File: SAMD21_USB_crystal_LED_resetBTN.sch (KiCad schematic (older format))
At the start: 13 parts

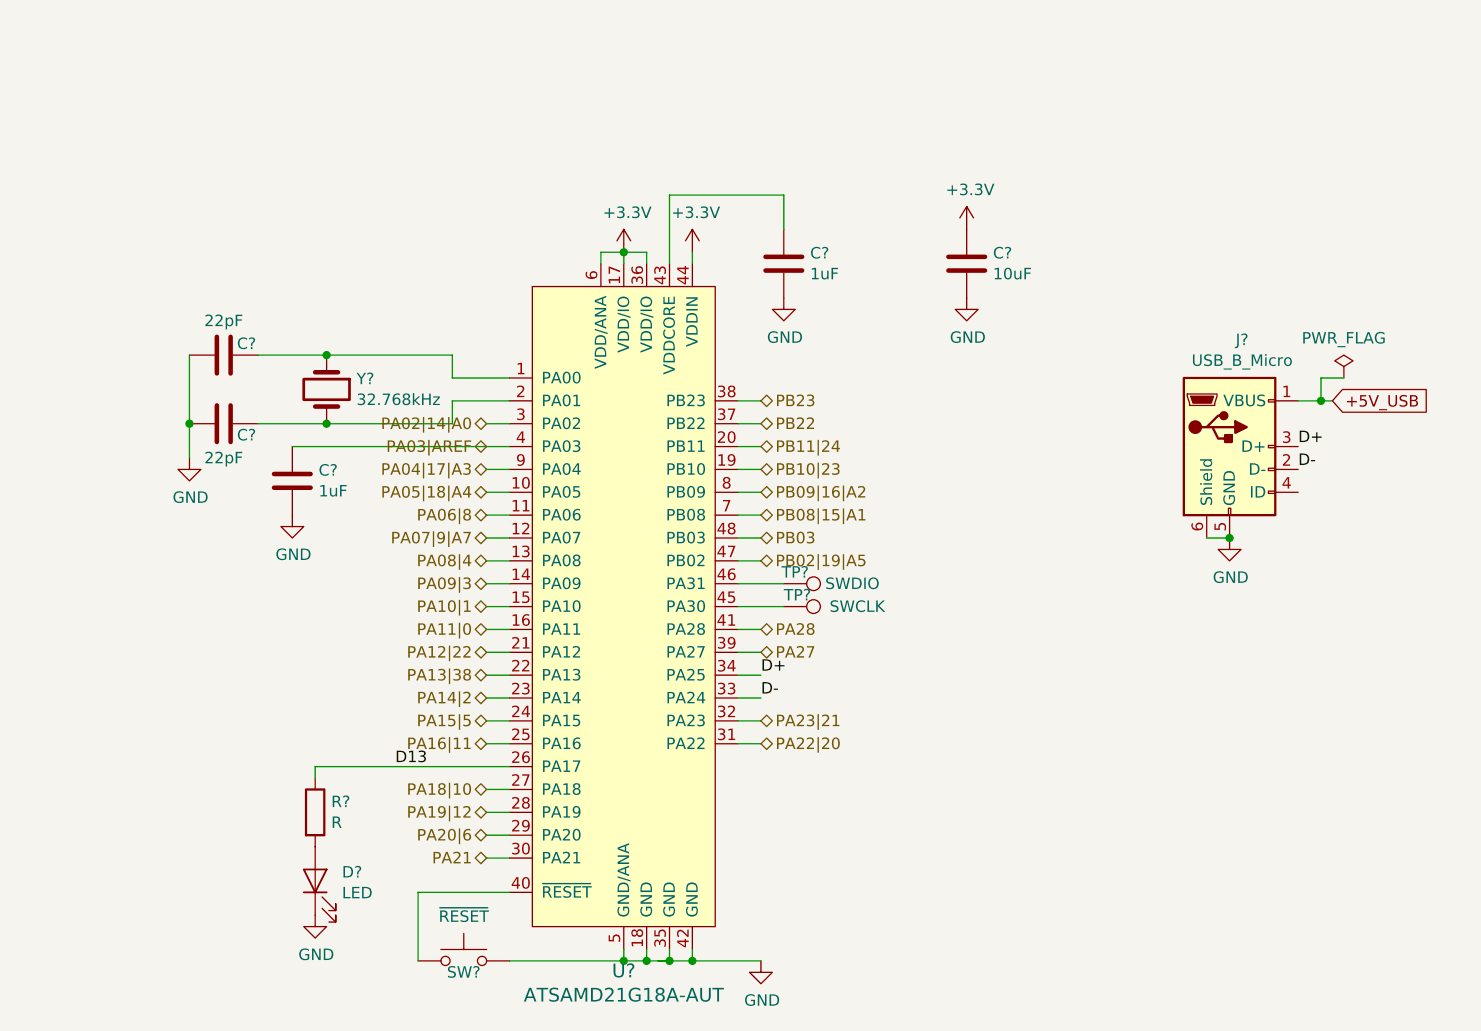
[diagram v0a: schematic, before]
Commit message: Add 3v3 LDO, annotate schematic
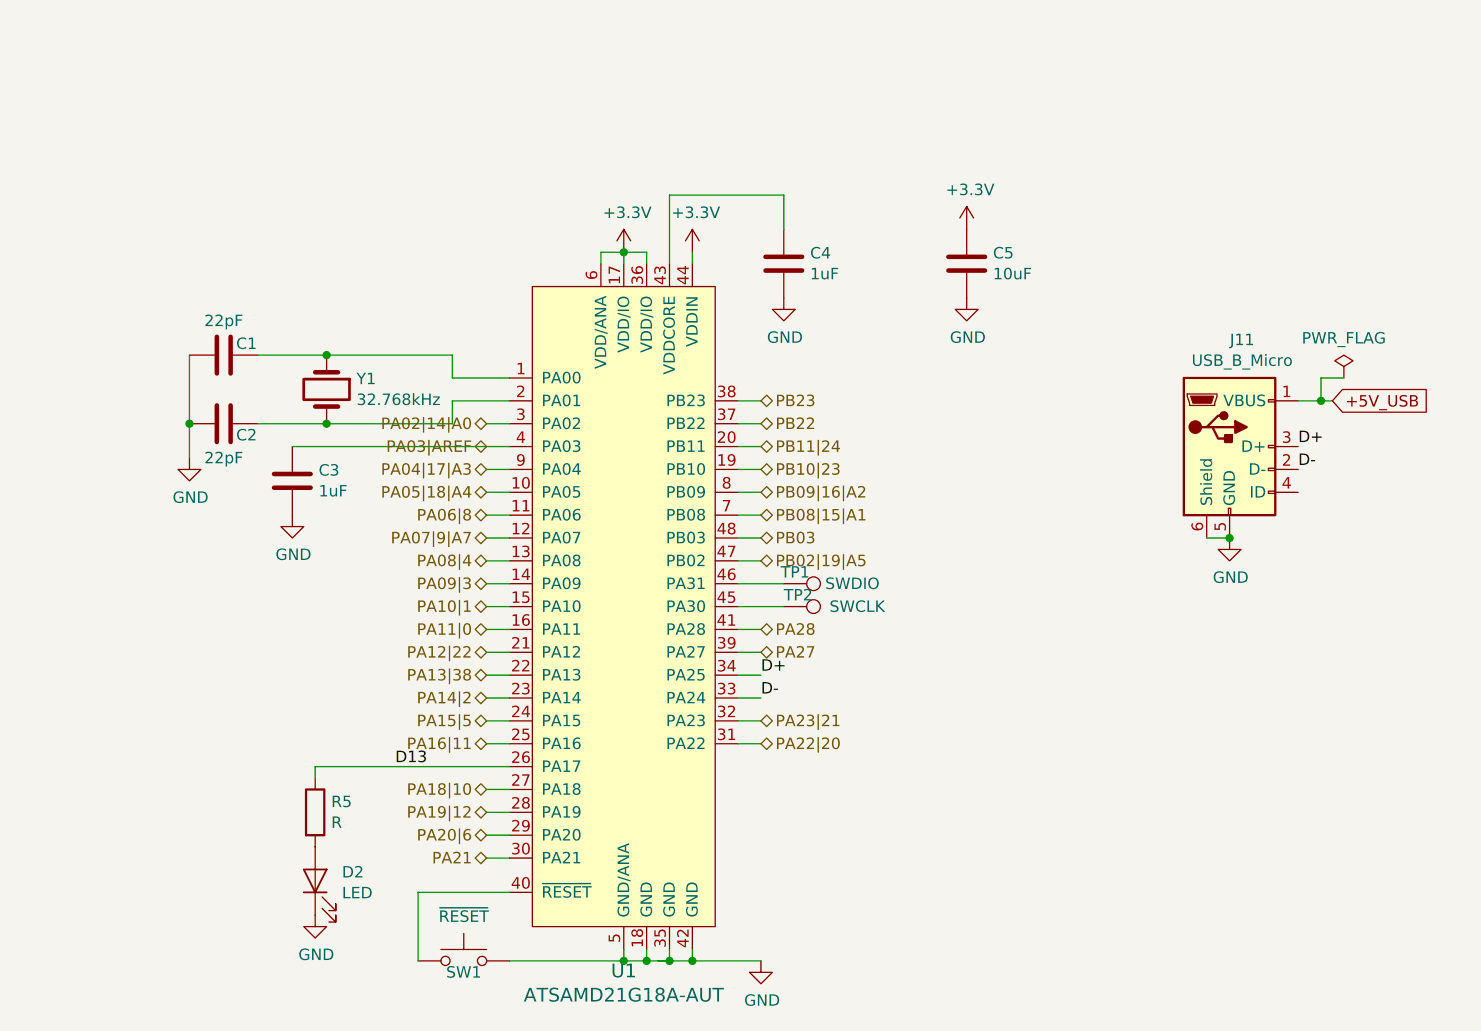
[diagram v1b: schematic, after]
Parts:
- gave numbers to parts that had none: 13
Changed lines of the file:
@@
 $EndDescr
 $Comp
-L dk_Embedded-Microcontrollers:ATSAMD21G18A-AUT U?
+L dk_Embedded-Microcontrollers:ATSAMD21G18A-AUT U1
 U 1 1 5C2CF1D3
 P 3250 3450
-F 0 "U?" H 3250 1956 60  0000 C CNN
+F 0 "U1" H 3250 1956 60  0000 C CNN
 F 1 "ATSAMD21G18A-AUT" H 3250 1850 60  0000 C CNN
 F 2 "digikey-footprints:TQFP-48_7x7mm" H 3450 3650 60  0001 L CNN
@@
 $EndComp
 $Comp
-L Device:Crystal Y?
+L Device:Crystal Y1
 U 1 1 5C2EFCE8
 P 1950 2400
-F 0 "Y?" V 1904 2531 50  0000 L CNN
+F 0 "Y1" V 1904 2531 50  0000 L CNN
 F 1 "32.768kHz" V 1995 2531 50  0000 L CNN
 F 2 "" H 1950 2400 50  0001 C CNN
@@
 $EndComp
 $Comp
-L Device:C C?
+L Device:C C1
 U 1 1 5C2EFD71
 P 1500 2250
-F 0 "C?" V 1450 2350 50  0000 C CNN
+F 0 "C1" V 1450 2350 50  0000 C CNN
 F 1 "22pF" V 1350 2250 50  0000 C CNN
 F 2 "" H 1538 2100 50  0001 C CNN
@@
 $EndComp
 $Comp
-L Device:C C?
+L Device:C C2
 U 1 1 5C2EFDDF
 P 1500 2550
-F 0 "C?" V 1550 2650 50  0000 C CNN
+F 0 "C2" V 1550 2650 50  0000 C CNN
 F 1 "22pF" V 1650 2550 50  0000 C CNN
 F 2 "" H 1538 2400 50  0001 C CNN
@@
 $EndComp
 $Comp
-L Device:C C?
+L Device:C C4
 U 1 1 5C2EFE2A
 P 3950 1850
-F 0 "C?" H 4065 1896 50  0000 L CNN
+F 0 "C4" H 4065 1896 50  0000 L CNN
 F 1 "1uF" H 4065 1805 50  0000 L CNN
 F 2 "" H 3988 1700 50  0001 C CNN
@@
 $EndComp
 $Comp
-L Device:C C?
+L Device:C C3
 U 1 1 5C2EFF65
 P 1800 2800
-F 0 "C?" H 1915 2846 50  0000 L CNN
+F 0 "C3" H 1915 2846 50  0000 L CNN
 F 1 "1uF" H 1915 2755 50  0000 L CNN
 F 2 "" H 1838 2650 50  0001 C CNN
@@
 $EndComp
 $Comp
-L Device:C C?
+L Device:C C5
 U 1 1 5C2F0015
 P 4750 1850
-F 0 "C?" H 4865 1896 50  0000 L CNN
+F 0 "C5" H 4865 1896 50  0000 L CNN
 F 1 "10uF" H 4865 1805 50  0000 L CNN
 F 2 "" H 4788 1700 50  0001 C CNN
@@
 $EndComp
 $Comp
-L Connector:USB_B_Micro J?
+L Connector:USB_B_Micro J11
 U 1 1 5C2F22A1
 P 5900 2650
-F 0 "J?" H 5955 3117 50  0000 C CNN
+F 0 "J11" H 5955 3117 50  0000 C CNN
 F 1 "USB_B_Micro" H 5955 3026 50  0000 C CNN
 F 2 "" H 6050 2600 50  0001 C CNN
@@
 $EndComp
 $Comp
-L Device:LED D?
+L Device:LED D2
 U 1 1 5C2F24D2
 P 1900 4550
-F 0 "D?" V 1938 4433 50  0000 R CNN
+F 0 "D2" V 1938 4433 50  0000 R CNN
 F 1 "LED" V 1847 4433 50  0000 R CNN
 F 2 "" H 1900 4550 50  0001 C CNN
@@
 $EndComp
 $Comp
-L Device:R R?
+L Device:R R5
 U 1 1 5C2F2611
 P 1900 4250
-F 0 "R?" H 1970 4296 50  0000 L CNN
+F 0 "R5" H 1970 4296 50  0000 L CNN
 F 1 "R" H 1970 4205 50  0000 L CNN
 F 2 "" V 1830 4250 50  0001 C CNN
@@
 $EndComp
 $Comp
-L Connector:TestPoint TP?
+L Connector:TestPoint TP1
 U 1 1 5C2F2731
 P 3950 3250
-F 0 "TP?" V 3900 3300 50  0000 C CNN
+F 0 "TP1" V 3900 3300 50  0000 C CNN
 F 1 "SWDIO" V 3950 3550 50  0000 C CNN
 F 2 "" H 4150 3250 50  0001 C CNN
@@
 $EndComp
 $Comp
-L Connector:TestPoint TP?
+L Connector:TestPoint TP2
 U 1 1 5C2F27EB
 P 3950 3350
-F 0 "TP?" V 3900 3350 50  0000 L CNN
+F 0 "TP2" V 3900 3350 50  0000 L CNN
 F 1 "SWCLK" V 3950 3550 50  0000 L CNN
 F 2 "" H 4150 3350 50  0001 C CNN
@@
 $EndComp
 $Comp
-L Switch:SW_Push SW?
+L Switch:SW_Push SW1
 U 1 1 5C2F8B84
 P 2550 4900
-F 0 "SW?" H 2550 4850 50  0000 C CNN
+F 0 "SW1" H 2550 4850 50  0000 C CNN
 F 1 "~RESET" H 2550 5094 50  0000 C CNN
 F 2 "" H 2550 5100 50  0001 C CNN

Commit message: Fix schematic ERC
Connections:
- no-connect marks 0 -> 1
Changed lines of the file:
@@
 Text GLabel 6350 2450 2    50   Input ~ 0
 +5V_USB
-Wire Wire Line
-	6200 2450 6300 2450
-$Comp
-L power:PWR_FLAG #FLG0101
-U 1 1 5C2F4820
-P 6400 2350
-F 0 "#FLG0101" H 6400 2425 50  0001 C CNN
-F 1 "PWR_FLAG" H 6400 2524 50  0000 C CNN
-F 2 "" H 6400 2350 50  0001 C CNN
-F 3 "~" H 6400 2350 50  0001 C CNN
-	1    6400 2350
-	1    0    0    -1
-$EndComp
-Wire Wire Line
-	6400 2350 6300 2350
-Wire Wire Line
-	6300 2350 6300 2450
-Connection ~ 6300 2450
-Wire Wire Line
-	6300 2450 6350 2450
 $Comp
 L power:GND #PWR0109
@@
 Wire Wire Line
 	3850 2550 3750 2550
-Wire Wire Line
-	3750 2650 3850 2650
-Wire Wire Line
-	3850 2750 3750 2750
-Wire Wire Line
-	3750 2850 3850 2850
 Text HLabel 2650 2650 0    50   BiDi ~ 0
 PA03|AREF
 Wire Wire Line
 	1800 2650 2750 2650
+Wire Wire Line
+	6200 2450 6350 2450
+NoConn ~ 6200 2850
+Wire Wire Line
+	3750 2650 3850 2650
+Wire Wire Line
+	3750 2750 3850 2750
+Wire Wire Line
+	3750 2850 3850 2850
 $EndSCHEMATC

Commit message: XCtal caps changed, all footprints assigned
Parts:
- C1, C2: value 22pF -> 8pF; footprint (none) -> Capacitor_SMD:C_0603_1608Metric
- C3, C4: footprint (none) -> Capacitor_SMD:C_0603_1608Metric
- C5: footprint (none) -> Capacitor_SMD:C_1206_3216Metric
- D2: footprint (none) -> LED_SMD:LED_0805_2012Metric
- J11: footprint (none) -> digikey-footprints:USB_Micro_B_Female_10118192
- R5: footprint (none) -> Resistor_SMD:R_0603_1608Metric
- SW1: footprint (none) -> Button_Switch_SMD:SW_SPST_SKQG_WithStem
- TP1, TP2: footprint (none) -> TestPoint:TestPoint_THTPad_D1.5mm_Drill0.7mm
- U1: footprint digikey-footprints:TQFP-48_7x7mm -> Package_DFN_QFN:QFN-48-1EP_7x7mm_P0.5mm_EP5.3x5.3mm
- Y1: footprint (none) -> Crystal:Crystal_SMD_3215-2Pin_3.2x1.5mm
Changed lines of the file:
@@
 F 0 "U1" H 3250 1956 60  0000 C CNN
 F 1 "ATSAMD21G18A-AUT" H 3250 1850 60  0000 C CNN
-F 2 "digikey-footprints:TQFP-48_7x7mm" H 3450 3650 60  0001 L CNN
+F 2 "Package_DFN_QFN:QFN-48-1EP_7x7mm_P0.5mm_EP5.3x5.3mm" H 3450 3650 60  0001 L CNN
 F 3 "http://www.microchip.com/mymicrochip/filehandler.aspx?ddocname=en605782" H 3450 3750 60  0001 L CNN
 F 4 "ATSAMD21G18A-AUTCT-ND" H 3450 3850 60  0001 L CNN "Digi-Key_PN"
@@
 F 0 "Y1" V 1904 2531 50  0000 L CNN
 F 1 "32.768kHz" V 1995 2531 50  0000 L CNN
-F 2 "" H 1950 2400 50  0001 C CNN
+F 2 "Crystal:Crystal_SMD_3215-2Pin_3.2x1.5mm" H 1950 2400 50  0001 C CNN
 F 3 "~" H 1950 2400 50  0001 C CNN
 	1    1950 2400
@@
 P 1500 2250
 F 0 "C1" V 1450 2350 50  0000 C CNN
-F 1 "22pF" V 1350 2250 50  0000 C CNN
-F 2 "" H 1538 2100 50  0001 C CNN
+F 1 "8pF" V 1350 2250 50  0000 C CNN
+F 2 "Capacitor_SMD:C_0603_1608Metric" H 1538 2100 50  0001 C CNN
 F 3 "~" H 1500 2250 50  0001 C CNN
 	1    1500 2250
@@
 P 1500 2550
 F 0 "C2" V 1550 2650 50  0000 C CNN
-F 1 "22pF" V 1650 2550 50  0000 C CNN
-F 2 "" H 1538 2400 50  0001 C CNN
+F 1 "8pF" V 1650 2550 50  0000 C CNN
+F 2 "Capacitor_SMD:C_0603_1608Metric" H 1538 2400 50  0001 C CNN
 F 3 "~" H 1500 2550 50  0001 C CNN
 	1    1500 2550
@@
 F 0 "C4" H 4065 1896 50  0000 L CNN
 F 1 "1uF" H 4065 1805 50  0000 L CNN
-F 2 "" H 3988 1700 50  0001 C CNN
+F 2 "Capacitor_SMD:C_0603_1608Metric" H 3988 1700 50  0001 C CNN
 F 3 "~" H 3950 1850 50  0001 C CNN
 	1    3950 1850
@@
 F 0 "C3" H 1915 2846 50  0000 L CNN
 F 1 "1uF" H 1915 2755 50  0000 L CNN
-F 2 "" H 1838 2650 50  0001 C CNN
+F 2 "Capacitor_SMD:C_0603_1608Metric" H 1838 2650 50  0001 C CNN
 F 3 "~" H 1800 2800 50  0001 C CNN
 	1    1800 2800
@@
 F 0 "C5" H 4865 1896 50  0000 L CNN
 F 1 "10uF" H 4865 1805 50  0000 L CNN
-F 2 "" H 4788 1700 50  0001 C CNN
+F 2 "Capacitor_SMD:C_1206_3216Metric" H 4788 1700 50  0001 C CNN
 F 3 "~" H 4750 1850 50  0001 C CNN
 	1    4750 1850
@@
 F 0 "J11" H 5955 3117 50  0000 C CNN
 F 1 "USB_B_Micro" H 5955 3026 50  0000 C CNN
-F 2 "" H 6050 2600 50  0001 C CNN
+F 2 "digikey-footprints:USB_Micro_B_Female_10118192" H 6050 2600 50  0001 C CNN
 F 3 "~" H 6050 2600 50  0001 C CNN
 	1    5900 2650
@@
 F 0 "D2" V 1938 4433 50  0000 R CNN
 F 1 "LED" V 1847 4433 50  0000 R CNN
-F 2 "" H 1900 4550 50  0001 C CNN
+F 2 "LED_SMD:LED_0805_2012Metric" H 1900 4550 50  0001 C CNN
 F 3 "~" H 1900 4550 50  0001 C CNN
 	1    1900 4550
@@
 F 0 "R5" H 1970 4296 50  0000 L CNN
 F 1 "R" H 1970 4205 50  0000 L CNN
-F 2 "" V 1830 4250 50  0001 C CNN
+F 2 "Resistor_SMD:R_0603_1608Metric" V 1830 4250 50  0001 C CNN
 F 3 "~" H 1900 4250 50  0001 C CNN
 	1    1900 4250
@@
 F 0 "TP1" V 3900 3300 50  0000 C CNN
 F 1 "SWDIO" V 3950 3550 50  0000 C CNN
-F 2 "" H 4150 3250 50  0001 C CNN
+F 2 "TestPoint:TestPoint_THTPad_D1.5mm_Drill0.7mm" H 4150 3250 50  0001 C CNN
 F 3 "~" H 4150 3250 50  0001 C CNN
 	1    3950 3250
@@
 F 0 "TP2" V 3900 3350 50  0000 L CNN
 F 1 "SWCLK" V 3950 3550 50  0000 L CNN
-F 2 "" H 4150 3350 50  0001 C CNN
+F 2 "TestPoint:TestPoint_THTPad_D1.5mm_Drill0.7mm" H 4150 3350 50  0001 C CNN
 F 3 "~" H 4150 3350 50  0001 C CNN
 	1    3950 3350
@@
 F 0 "SW1" H 2550 4850 50  0000 C CNN
 F 1 "~RESET" H 2550 5094 50  0000 C CNN
-F 2 "" H 2550 5100 50  0001 C CNN
+F 2 "Button_Switch_SMD:SW_SPST_SKQG_WithStem" H 2550 5100 50  0001 C CNN
 F 3 "" H 2550 5100 50  0001 C CNN
 	1    2550 4900

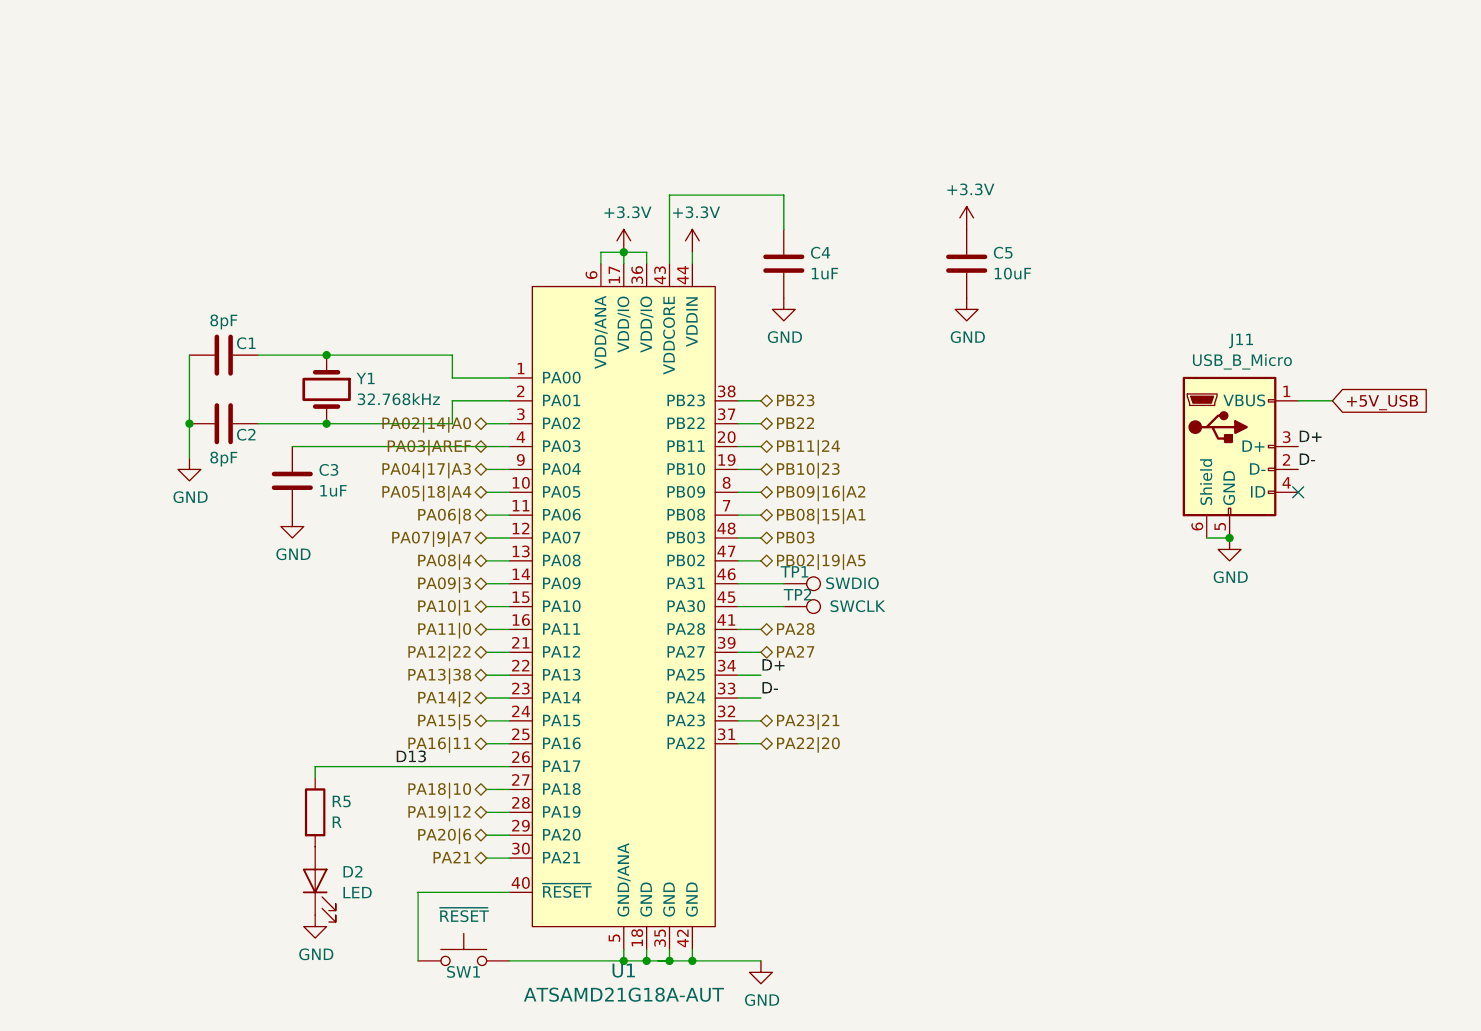
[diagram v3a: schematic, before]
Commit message: Add MCU caps, test points, SWDCLK pull-up; validate ERC and checklist
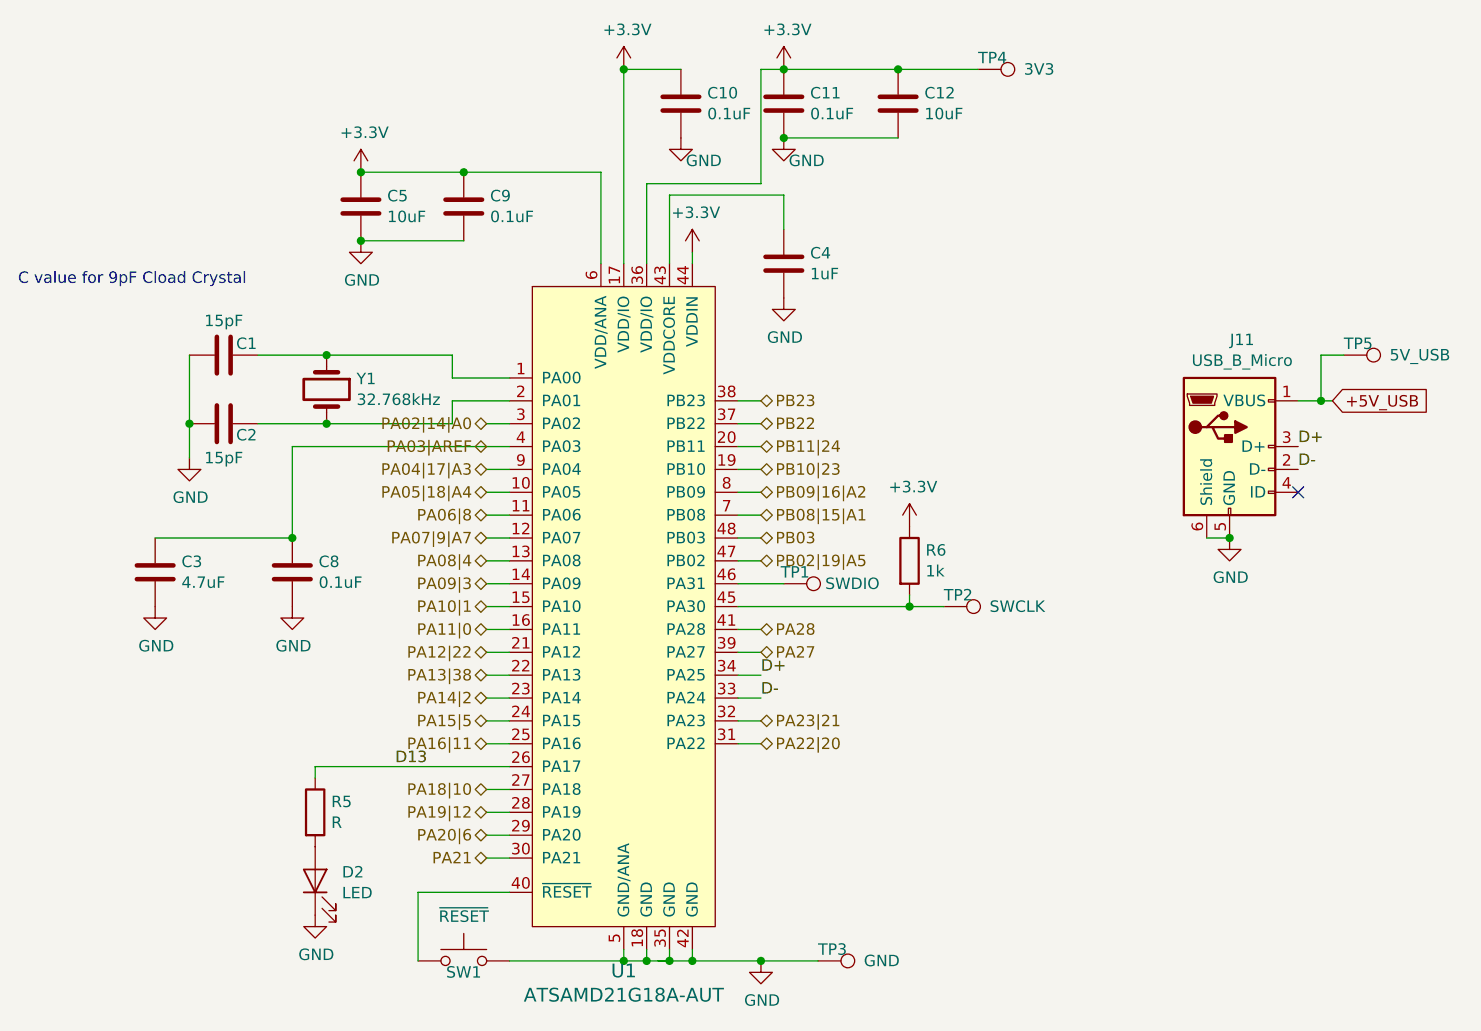
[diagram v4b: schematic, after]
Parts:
- added C10, C11, C8, C9: 0.1uF, Capacitor_SMD:C_0603_1608Metric, symbol Device:C
- added C12: 10uF, Capacitor_SMD:C_1206_3216Metric, symbol Device:C
- added R6: 1k, Resistor_SMD:R_0603_1608Metric, symbol Device:R
- added TP3: GND, TestPoint:TestPoint_THTPad_D1.5mm_Drill0.7mm, symbol Connector:TestPoint
- added TP4: 3V3, TestPoint:TestPoint_THTPad_D1.5mm_Drill0.7mm, symbol Connector:TestPoint
- added TP5: 5V_USB, TestPoint:TestPoint_THTPad_D1.5mm_Drill0.7mm, symbol Connector:TestPoint
- C1, C2: value 8pF -> 15pF
- C3: value 1uF -> 4.7uF
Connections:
- net +3V3: now also C10.1, C11.1, C12.1, C9.1, R6.1, TP4.1
- net +5V_USB: now also TP5.1
- net GND: now also C10.2, C11.2, C12.2, C8.2, C9.2, TP3.1
- net PA03|AREF: now also C8.1
- net at TP2.1, U1.45 (PA30): now also R6.2
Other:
- note added: "C value for 9pF Cload Crystal"
- moved on the sheet: C3, C5, TP2

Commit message: Replace header with 0.1" and 0805 capacitor
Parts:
- C3: footprint Capacitor_SMD:C_0603_1608Metric -> Capacitor_SMD:C_0805_2012Metric
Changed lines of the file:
@@
 F 0 "C3" H 1315 3246 50  0000 L CNN
 F 1 "4.7uF" H 1315 3155 50  0000 L CNN
-F 2 "Capacitor_SMD:C_0603_1608Metric" H 1238 3050 50  0001 C CNN
+F 2 "Capacitor_SMD:C_0805_2012Metric" H 1238 3050 50  0001 C CNN
 F 3 "~" H 1200 3200 50  0001 C CNN
 	1    1200 3200
